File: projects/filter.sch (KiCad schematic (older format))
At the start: 24 parts, among them U601 OPA1632, U602 OPA1632

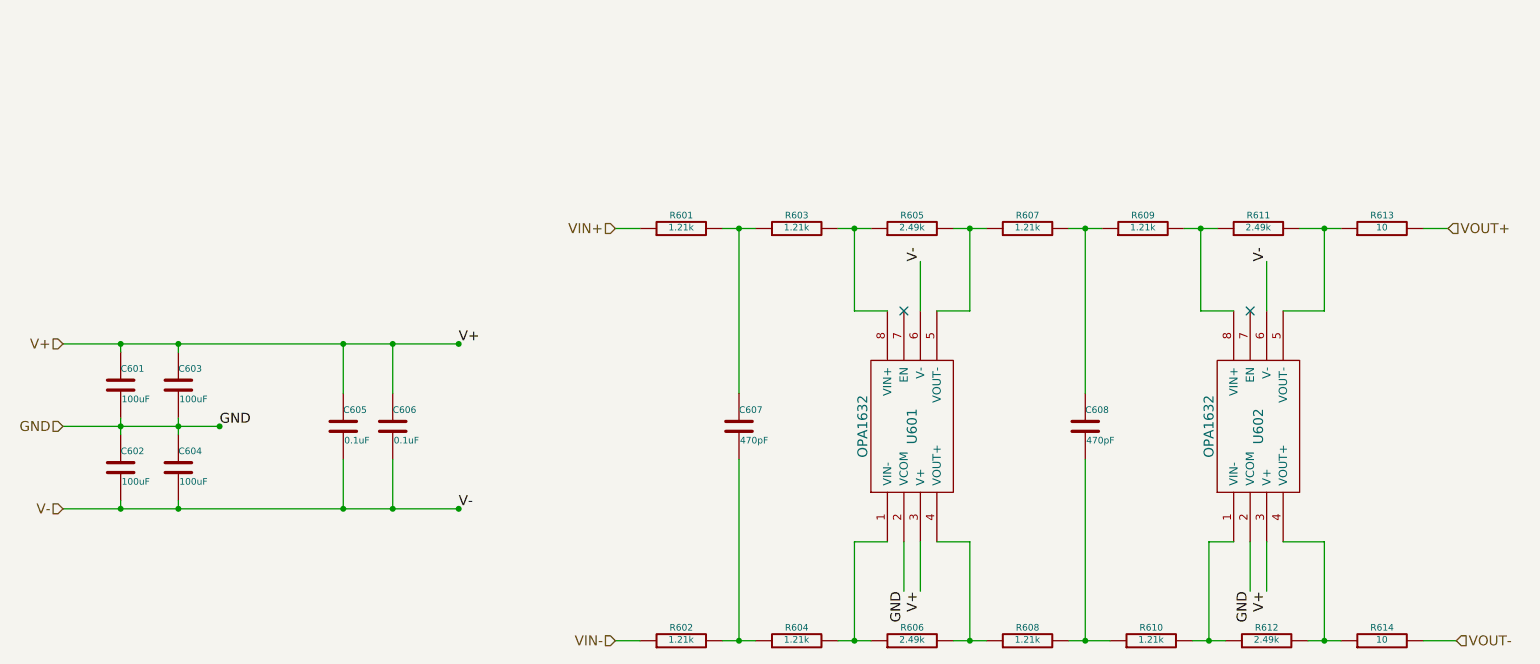
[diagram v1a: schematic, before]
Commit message: add box cap and small electrolytic cap footprints
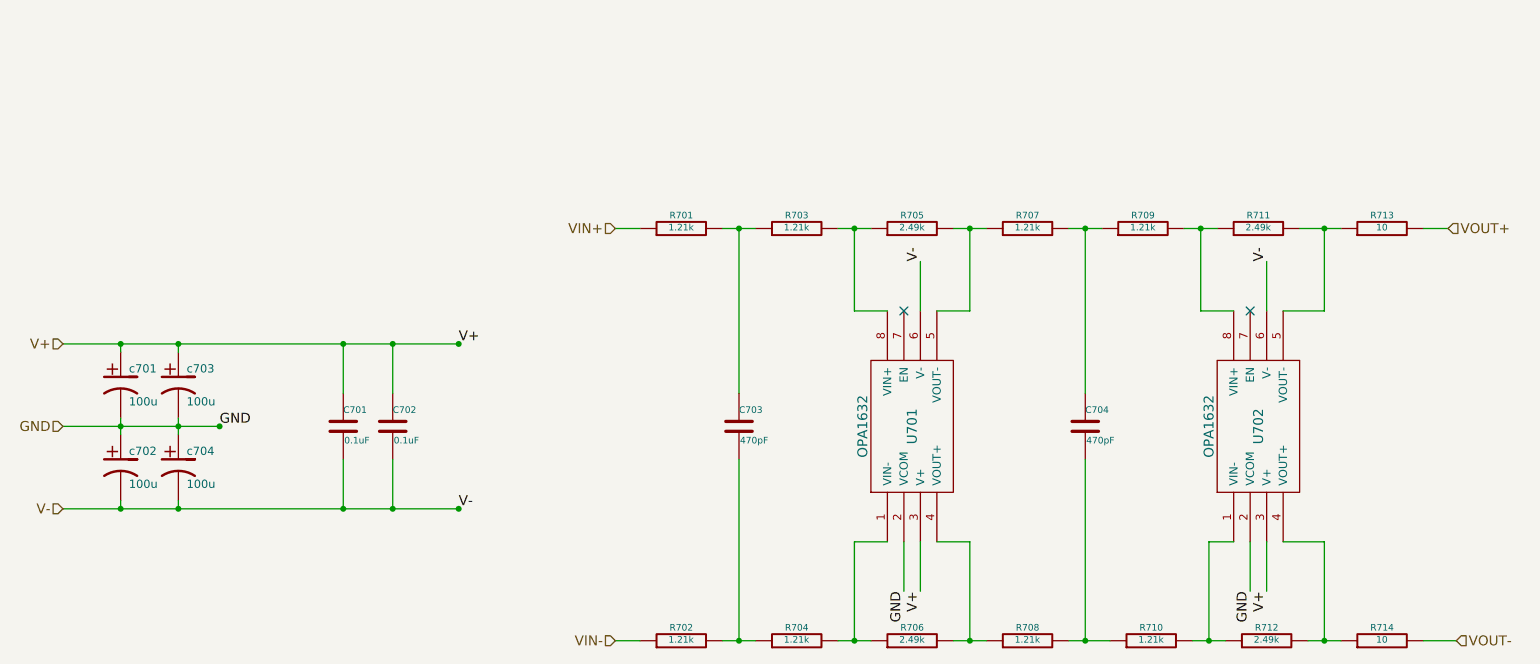
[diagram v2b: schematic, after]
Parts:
- removed C601, C602, C603, C604: 100uF, symbol C
- added c601, c602, c603, c604: 100u, symbol CP1
- renumbered C605 to C601, C606 to C602, C607 to C603, C608 to C604
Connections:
- net GND: now also c601.2, c602.1, c603.2, c604.1
- net V+: now also c601.1, c603.1
- net V-: now also c602.2, c604.2
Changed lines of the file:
@@
 GND
 $Comp
-L C C607
+L C C603
 U 1 1 5428A511
 P 5850 3900
-AR Path="/541690F5/5428A511" Ref="C607"  Part="1"
-AR Path="/5428BABE/5428A511" Ref="C707"  Part="1"
-F 0 "C607" H 5850 4000 40  0000 L CNN
+AR Path="/541690F5/5428A511" Ref="C603"  Part="1"
+AR Path="/5428BABE/5428A511" Ref="C703"  Part="1"
+F 0 "C703" H 5850 4000 40  0000 L CNN
 F 1 "470pF" H 5856 3815 40  0000 L CNN
 F 2 "" H 5888 3750 30  0000 C CNN
@@
 AR Path="/541690F5/5428A539" Ref="R601"  Part="1"
 AR Path="/5428BABE/5428A539" Ref="R701"  Part="1"
-F 0 "R601" V 5580 2700 40  0000 C CNN
+F 0 "R701" V 5580 2700 40  0000 C CNN
 F 1 "1.21k" V 5507 2701 40  0000 C CNN
 F 2 "" V 5430 2700 30  0000 C CNN
@@
 AR Path="/541690F5/5428B1BE" Ref="R605"  Part="1"
 AR Path="/5428BABE/5428B1BE" Ref="R705"  Part="1"
-F 0 "R605" V 6980 2700 40  0000 C CNN
+F 0 "R705" V 6980 2700 40  0000 C CNN
 F 1 "2.49k" V 6907 2701 40  0000 C CNN
 F 2 "" V 6830 2700 30  0000 C CNN
@@
 AR Path="/541690F5/5428B212" Ref="R613"  Part="1"
 AR Path="/5428BABE/5428B212" Ref="R713"  Part="1"
-F 0 "R613" V 9830 2700 40  0000 C CNN
+F 0 "R713" V 9830 2700 40  0000 C CNN
 F 1 "10" V 9757 2701 40  0000 C CNN
 F 2 "" V 9680 2700 30  0000 C CNN
@@
 AR Path="/541690F5/5431C69B" Ref="U601"  Part="1"
 AR Path="/5428BABE/5431C69B" Ref="U701"  Part="1"
-F 0 "U601" H 6900 3900 60  0000 C CNN
+F 0 "U701" H 6900 3900 60  0000 C CNN
 F 1 "OPA1632" H 6900 4200 60  0000 C CNN
 F 2 "" H 6900 3700 60  0000 C CNN
@@
 AR Path="/541690F5/5431C6F1" Ref="U602"  Part="1"
 AR Path="/5428BABE/5431C6F1" Ref="U702"  Part="1"
-F 0 "U602" H 9000 3900 60  0000 C CNN
+F 0 "U702" H 9000 3900 60  0000 C CNN
 F 1 "OPA1632" H 9000 4200 60  0000 C CNN
 F 2 "" H 9000 3700 60  0000 C CNN
@@
 AR Path="/541690F5/5431DA55" Ref="R603"  Part="1"
 AR Path="/5428BABE/5431DA55" Ref="R703"  Part="1"
-F 0 "R603" V 6280 2700 40  0000 C CNN
+F 0 "R703" V 6280 2700 40  0000 C CNN
 F 1 "1.21k" V 6207 2701 40  0000 C CNN
 F 2 "" V 6130 2700 30  0000 C CNN
@@
 AR Path="/541690F5/5431DA6A" Ref="R607"  Part="1"
 AR Path="/5428BABE/5431DA6A" Ref="R707"  Part="1"
-F 0 "R607" V 7680 2700 40  0000 C CNN
+F 0 "R707" V 7680 2700 40  0000 C CNN
 F 1 "1.21k" V 7607 2701 40  0000 C CNN
 F 2 "" V 7530 2700 30  0000 C CNN
@@
 AR Path="/541690F5/5431DA7F" Ref="R609"  Part="1"
 AR Path="/5428BABE/5431DA7F" Ref="R709"  Part="1"
-F 0 "R609" V 8380 2700 40  0000 C CNN
+F 0 "R709" V 8380 2700 40  0000 C CNN
 F 1 "1.21k" V 8307 2701 40  0000 C CNN
 F 2 "" V 8230 2700 30  0000 C CNN
@@
 AR Path="/541690F5/5431DA94" Ref="R611"  Part="1"
 AR Path="/5428BABE/5431DA94" Ref="R711"  Part="1"
-F 0 "R611" V 9080 2700 40  0000 C CNN
+F 0 "R711" V 9080 2700 40  0000 C CNN
 F 1 "2.49k" V 9007 2701 40  0000 C CNN
 F 2 "" V 8930 2700 30  0000 C CNN
@@
 AR Path="/541690F5/5431DAA9" Ref="R602"  Part="1"
 AR Path="/5428BABE/5431DAA9" Ref="R702"  Part="1"
-F 0 "R602" V 5580 5200 40  0000 C CNN
+F 0 "R702" V 5580 5200 40  0000 C CNN
 F 1 "1.21k" V 5507 5201 40  0000 C CNN
 F 2 "" V 5430 5200 30  0000 C CNN
@@
 AR Path="/541690F5/5431DABE" Ref="R604"  Part="1"
 AR Path="/5428BABE/5431DABE" Ref="R704"  Part="1"
-F 0 "R604" V 6280 5200 40  0000 C CNN
+F 0 "R704" V 6280 5200 40  0000 C CNN
 F 1 "1.21k" V 6207 5201 40  0000 C CNN
 F 2 "" V 6130 5200 30  0000 C CNN
@@
 AR Path="/541690F5/5431DB2C" Ref="R606"  Part="1"
 AR Path="/5428BABE/5431DB2C" Ref="R706"  Part="1"
-F 0 "R606" V 6980 5200 40  0000 C CNN
+F 0 "R706" V 6980 5200 40  0000 C CNN
 F 1 "2.49k" V 6907 5201 40  0000 C CNN
 F 2 "" V 6830 5200 30  0000 C CNN
@@
 AR Path="/541690F5/5431DB41" Ref="R608"  Part="1"
 AR Path="/5428BABE/5431DB41" Ref="R708"  Part="1"
-F 0 "R608" V 7680 5200 40  0000 C CNN
+F 0 "R708" V 7680 5200 40  0000 C CNN
 F 1 "1.21k" V 7607 5201 40  0000 C CNN
 F 2 "" V 7530 5200 30  0000 C CNN
@@
 AR Path="/541690F5/5431DB56" Ref="R610"  Part="1"
 AR Path="/5428BABE/5431DB56" Ref="R710"  Part="1"
-F 0 "R610" V 8430 5200 40  0000 C CNN
+F 0 "R710" V 8430 5200 40  0000 C CNN
 F 1 "1.21k" V 8357 5201 40  0000 C CNN
 F 2 "" V 8280 5200 30  0000 C CNN
@@
 AR Path="/541690F5/5431DB6B" Ref="R612"  Part="1"
 AR Path="/5428BABE/5431DB6B" Ref="R712"  Part="1"
-F 0 "R612" V 9130 5200 40  0000 C CNN
+F 0 "R712" V 9130 5200 40  0000 C CNN
 F 1 "2.49k" V 9057 5201 40  0000 C CNN
 F 2 "" V 8980 5200 30  0000 C CNN
@@
 $EndComp
 $Comp
-L C C608
+L C C604
 U 1 1 5431DDDC
 P 7950 3900
-AR Path="/541690F5/5431DDDC" Ref="C608"  Part="1"
-AR Path="/5428BABE/5431DDDC" Ref="C708"  Part="1"
-F 0 "C608" H 7950 4000 40  0000 L CNN
+AR Path="/541690F5/5431DDDC" Ref="C604"  Part="1"
+AR Path="/5428BABE/5431DDDC" Ref="C704"  Part="1"
+F 0 "C704" H 7950 4000 40  0000 L CNN
 F 1 "470pF" H 7956 3815 40  0000 L CNN
 F 2 "" H 7988 3750 30  0000 C CNN
@@
 AR Path="/541690F5/5431E4D7" Ref="R614"  Part="1"
 AR Path="/5428BABE/5431E4D7" Ref="R714"  Part="1"
-F 0 "R614" V 9830 5200 40  0000 C CNN
+F 0 "R714" V 9830 5200 40  0000 C CNN
 F 1 "10" V 9757 5201 40  0000 C CNN
 F 2 "" V 9680 5200 30  0000 C CNN
@@
 $Comp
 L C C601
-U 1 1 543A32F8
-P 2100 3650
-AR Path="/541690F5/543A32F8" Ref="C601"  Part="1"
-AR Path="/5428BABE/543A32F8" Ref="C701"  Part="1"
-F 0 "C601" H 2100 3750 40  0000 L CNN
-F 1 "100uF" H 2106 3565 40  0000 L CNN
-F 2 "" H 2138 3500 30  0000 C CNN
-F 3 "" H 2100 3650 60  0000 C CNN
-F 4 "Digi-Key" H 2100 3650 60  0001 C CNN "Supplier"
-F 5 "P16291-ND" H 2100 3650 60  0001 C CNN "Supplier-PN"
-F 6 "Panasonic" H 2100 3650 60  0001 C CNN "Manu"
-F 7 "16SEPC100M" H 2100 3650 60  0001 C CNN "Manu-PN"
-F 8 "CAP ALUM 100UF 16V 20% RADIAL" H 2100 3650 60  0001 C CNN "Description"
-	1    2100 3650
-	1    0    0    -1
-$EndComp
-$Comp
-L C C605
 U 1 1 543A33EF
 P 3450 3900
-AR Path="/541690F5/543A33EF" Ref="C605"  Part="1"
-AR Path="/5428BABE/543A33EF" Ref="C705"  Part="1"
-F 0 "C605" H 3450 4000 40  0000 L CNN
+AR Path="/541690F5/543A33EF" Ref="C601"  Part="1"
+AR Path="/5428BABE/543A33EF" Ref="C701"  Part="1"
+F 0 "C701" H 3450 4000 40  0000 L CNN
 F 1 "0.1uF" H 3456 3815 40  0000 L CNN
 F 2 "" H 3488 3750 30  0000 C CNN
@@
 Connection ~ 2450 4400
 $Comp
-L C C606
+L C C602
 U 1 1 5449F9E9
 P 3750 3900
-AR Path="/541690F5/5449F9E9" Ref="C606"  Part="1"
-AR Path="/5428BABE/5449F9E9" Ref="C706"  Part="1"
-F 0 "C606" H 3750 4000 40  0000 L CNN
+AR Path="/541690F5/5449F9E9" Ref="C602"  Part="1"
+AR Path="/5428BABE/5449F9E9" Ref="C702"  Part="1"
+F 0 "C702" H 3750 4000 40  0000 L CNN
 F 1 "0.1uF" H 3756 3815 40  0000 L CNN
 F 2 "" H 3788 3750 30  0000 C CNN
@@
 $EndComp
 $Comp
-L C C603
-U 1 1 5449FA42
+L CP1 c601
+U 1 1 548575CB
+P 2100 3650
+AR Path="/541690F5/548575CB" Ref="c601"  Part="1"
+AR Path="/5428BABE/548575CB" Ref="c701"  Part="1"
+F 0 "c701" H 2150 3750 50  0000 L CNN
+F 1 "100u" H 2150 3550 50  0000 L CNN
+F 2 "" H 2100 3650 60  0000 C CNN
+F 3 "" H 2100 3650 60  0000 C CNN
+F 4 "Digi-key" H 2100 3650 60  0001 C CNN "Supplier"
+F 5 "P16291-ND" H 2100 3650 60  0001 C CNN "Supplier-PN"
+F 6 "Panasonic" H 2100 3650 60  0001 C CNN "Manu"
+F 7 "16SEPC100M" H 2100 3650 60  0001 C CNN "Manu-PN"
+F 8 "CAP ALUM 100UF 16V 20% RADIAL" H 2100 3650 60  0001 C CNN "Description"
+	1    2100 3650
+	1    0    0    -1
+$EndComp
+$Comp
+L CP1 c602
+U 1 1 54857740
+P 2100 4150
+AR Path="/541690F5/54857740" Ref="c602"  Part="1"
+AR Path="/5428BABE/54857740" Ref="c702"  Part="1"
+F 0 "c702" H 2150 4250 50  0000 L CNN
+F 1 "100u" H 2150 4050 50  0000 L CNN
+F 2 "" H 2100 4150 60  0000 C CNN
+F 3 "" H 2100 4150 60  0000 C CNN
+F 4 "Digi-key" H 2100 4150 60  0001 C CNN "Supplier"
+F 5 "P16291-ND" H 2100 4150 60  0001 C CNN "Supplier-PN"
+F 6 "Panasonic" H 2100 4150 60  0001 C CNN "Manu"
+F 7 "16SEPC100M" H 2100 4150 60  0001 C CNN "Manu-PN"
+F 8 "CAP ALUM 100UF 16V 20% RADIAL" H 2100 4150 60  0001 C CNN "Description"
+	1    2100 4150
+	1    0    0    -1
+$EndComp
+$Comp
+L CP1 c603
+U 1 1 54857755
 P 2450 3650
-AR Path="/541690F5/5449FA42" Ref="C603"  Part="1"
-AR Path="/5428BABE/5449FA42" Ref="C703"  Part="1"
-F 0 "C603" H 2450 3750 40  0000 L CNN
-F 1 "100uF" H 2456 3565 40  0000 L CNN
-F 2 "" H 2488 3500 30  0000 C CNN
+AR Path="/541690F5/54857755" Ref="c603"  Part="1"
+AR Path="/5428BABE/54857755" Ref="c703"  Part="1"
+F 0 "c703" H 2500 3750 50  0000 L CNN
+F 1 "100u" H 2500 3550 50  0000 L CNN
+F 2 "" H 2450 3650 60  0000 C CNN
 F 3 "" H 2450 3650 60  0000 C CNN
-F 4 "Digi-Key" H 2450 3650 60  0001 C CNN "Supplier"
+F 4 "Digi-key" H 2450 3650 60  0001 C CNN "Supplier"
 F 5 "P16291-ND" H 2450 3650 60  0001 C CNN "Supplier-PN"
 F 6 "Panasonic" H 2450 3650 60  0001 C CNN "Manu"
@@
 $EndComp
 $Comp
-L C C602
-U 1 1 5449FA57
-P 2100 4150
-AR Path="/541690F5/5449FA57" Ref="C602"  Part="1"
-AR Path="/5428BABE/5449FA57" Ref="C702"  Part="1"
-F 0 "C602" H 2100 4250 40  0000 L CNN
-F 1 "100uF" H 2106 4065 40  0000 L CNN
-F 2 "" H 2138 4000 30  0000 C CNN
-F 3 "" H 2100 4150 60  0000 C CNN
-F 4 "Digi-Key" H 2100 4150 60  0001 C CNN "Supplier"
-F 5 "P16291-ND" H 2100 4150 60  0001 C CNN "Supplier-PN"
-F 6 "Panasonic" H 2100 4150 60  0001 C CNN "Manu"
-F 7 "16SEPC100M" H 2100 4150 60  0001 C CNN "Manu-PN"
-F 8 "CAP ALUM 100UF 16V 20% RADIAL" H 2100 4150 60  0001 C CNN "Description"
-	1    2100 4150
-	1    0    0    -1
-$EndComp
-$Comp
-L C C604
-U 1 1 5449FA6C
+L CP1 c604
+U 1 1 5485776A
 P 2450 4150
-AR Path="/541690F5/5449FA6C" Ref="C604"  Part="1"
-AR Path="/5428BABE/5449FA6C" Ref="C704"  Part="1"
-F 0 "C604" H 2450 4250 40  0000 L CNN
-F 1 "100uF" H 2456 4065 40  0000 L CNN
-F 2 "" H 2488 4000 30  0000 C CNN
+AR Path="/541690F5/5485776A" Ref="c604"  Part="1"
+AR Path="/5428BABE/5485776A" Ref="c704"  Part="1"
+F 0 "c704" H 2500 4250 50  0000 L CNN
+F 1 "100u" H 2500 4050 50  0000 L CNN
+F 2 "" H 2450 4150 60  0000 C CNN
 F 3 "" H 2450 4150 60  0000 C CNN
-F 4 "Digi-Key" H 2450 4150 60  0001 C CNN "Supplier"
+F 4 "Digi-key" H 2450 4150 60  0001 C CNN "Supplier"
 F 5 "P16291-ND" H 2450 4150 60  0001 C CNN "Supplier-PN"
 F 6 "Panasonic" H 2450 4150 60  0001 C CNN "Manu"
